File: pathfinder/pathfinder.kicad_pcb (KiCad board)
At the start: 2 copper layers, 73 x 42 mm, 15 parts, among them SW1 SW_Push, SW2 SW_Push, SW3 SW_Push, SW4 SW_Push, U1 XIAO-RP2040-DIP

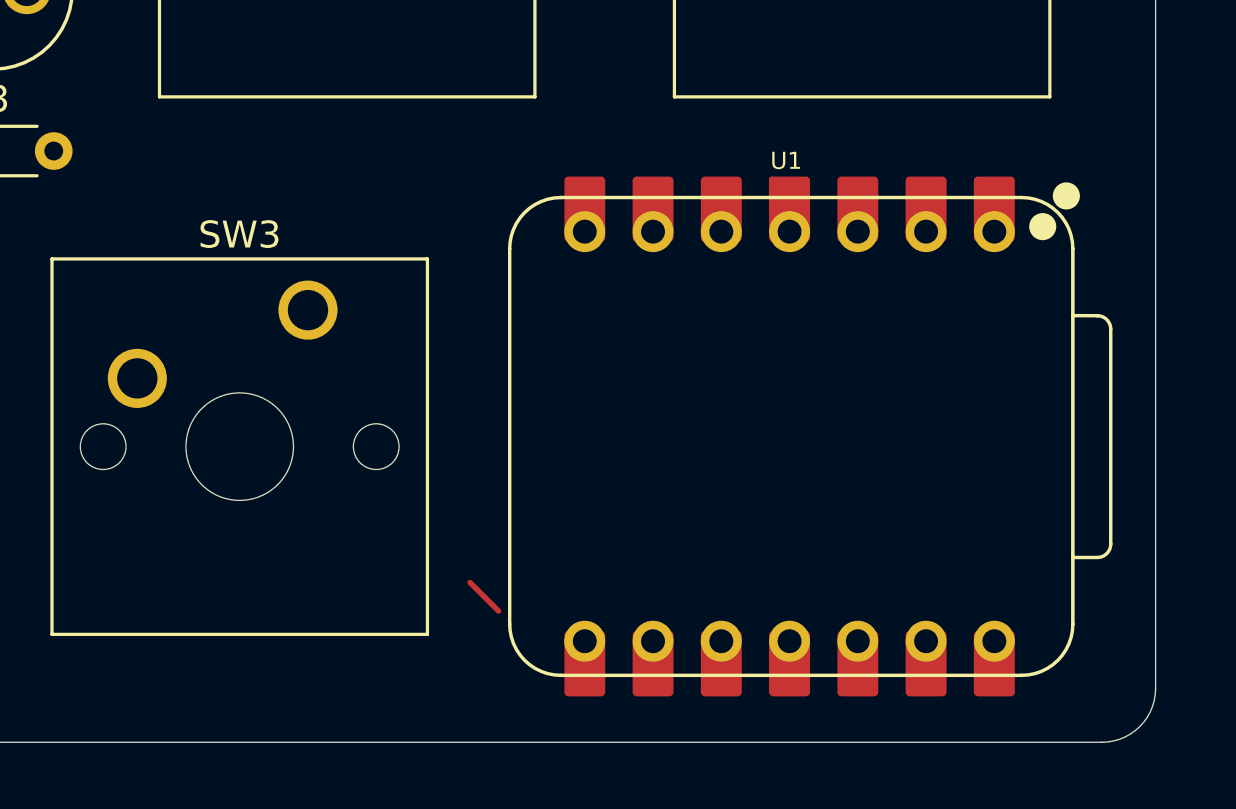
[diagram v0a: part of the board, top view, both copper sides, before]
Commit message: added silkscreen
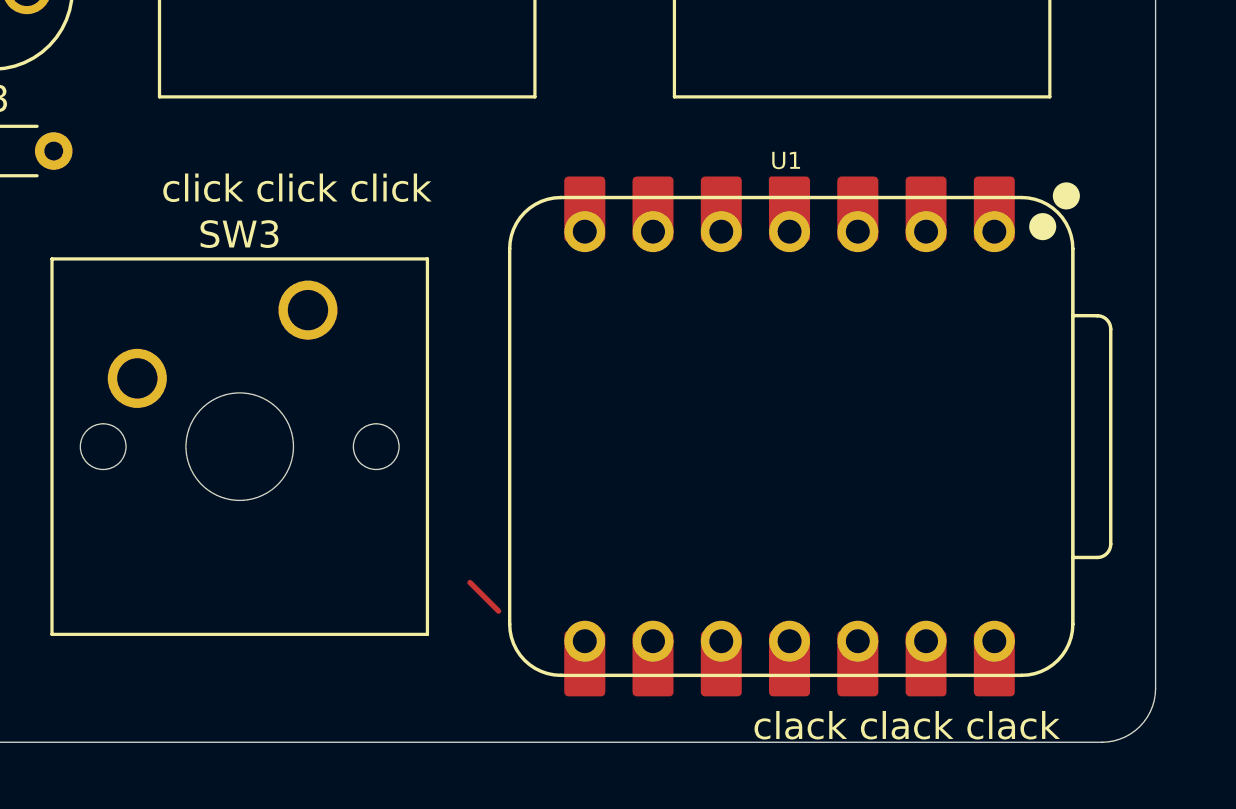
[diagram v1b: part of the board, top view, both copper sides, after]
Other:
- board text added: "clack clack clack"
- board text added: "click click click"
- board text added: "fidget"
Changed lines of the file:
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@@
 		(layer "Edge.Cuts")
+	)
+	(gr_text "click click click"
+		(at 131 48 0)
+		(layer "F.SilkS")
+		(effects
+			(font
+				(size 1 1)
+				(thickness 0.1)
+			)
+			(justify left bottom)
+		)
+	)
+	(gr_text "clack clack clack"
+		(at 153 68 0)
+		(layer "F.SilkS")
+		(effects
+			(font
+				(size 1 1)
+				(thickness 0.1)
+			)
+			(justify left bottom)
+		)
+	)
+	(gr_text "fidget"
+		(at 167 29 0)
+		(layer "B.SilkS")
+		(effects
+			(font
+				(size 2 2)
+				(thickness 0.2)
+			)
+			(justify left bottom mirror)
+		)
 	)
 	(segment
@@
 	)
 	(segment
+		(start 142.4895 62.058)
+		(end 143.5515 63.12)
+		(width 0.2)
+		(layer "F.Cu")
+		(net "led5")
+	)
+	(segment
 		(start 153.7115 47.045)
 		(end 153.7115 47.88)
@@
 		(net "Net-(D4-PadA)")
 	)
-	(segment
-		(start 142.4895 62.058)
-		(end 143.5515 63.12)
-		(width 0.2)
-		(layer "F.Cu")
-		(net "led5")
-	)
 	(embedded_fonts no)
